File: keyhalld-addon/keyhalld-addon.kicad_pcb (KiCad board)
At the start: 2 copper layers, 44 parts, among them J1 Conn_01x06_Pin, J2 Conn_01x04_Pin, SW1 SW_Push, SW2 SW_Push, SW3 SW_Push, SW4 SW_Push, SW5 SW_Push, SW6 SW_Push, SW7 SW_Push, SW8 SW_Push, U1 RP2350A, U2 ER_OLEDM0.91_1x-I2C, U22 TLV1117-33, Y1 12MHz

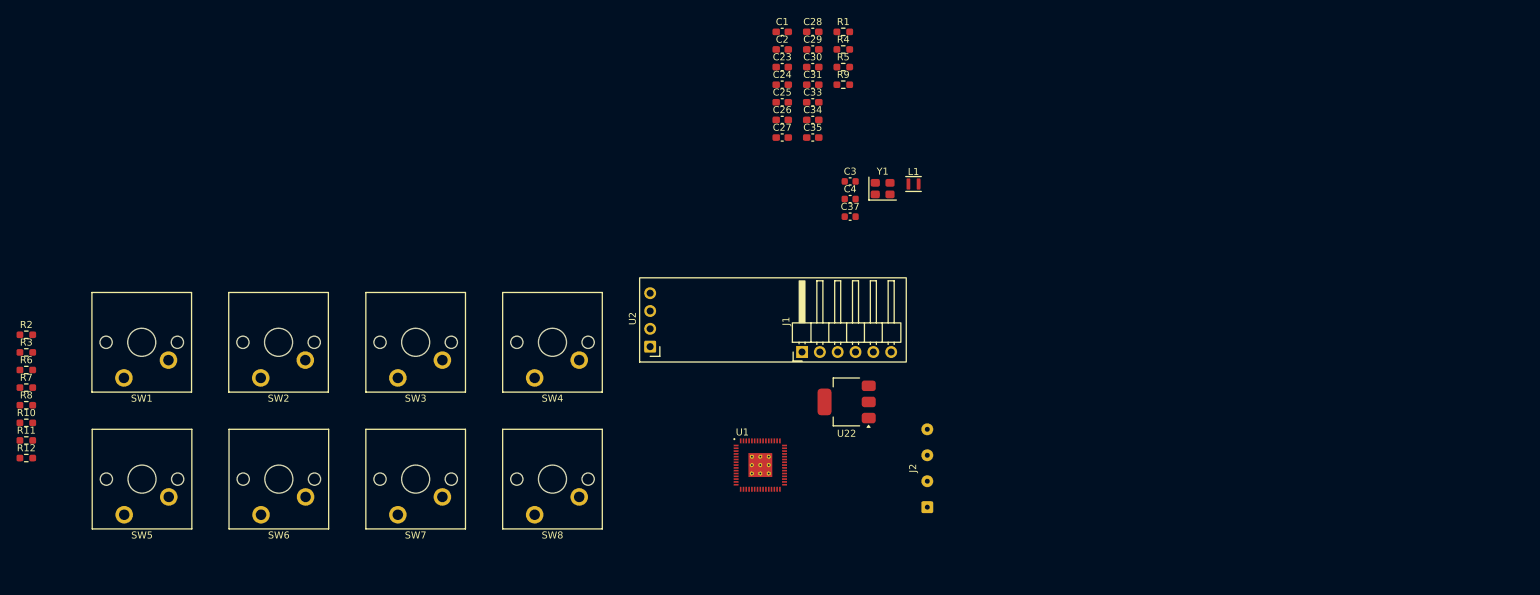
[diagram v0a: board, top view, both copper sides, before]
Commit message: add local fp for cherry mx mech switch
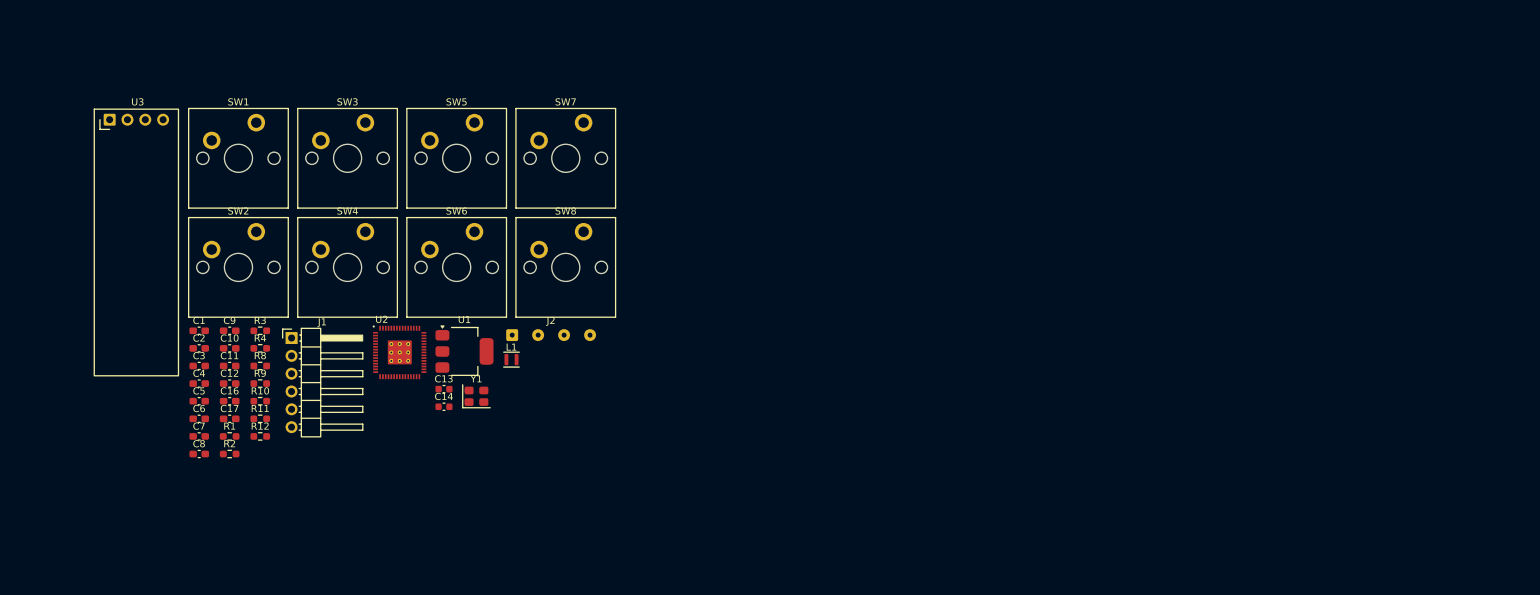
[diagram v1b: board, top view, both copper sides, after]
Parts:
- removed C23, C24, C25, C26, C27, C28, C29, C30, C33, C34: 100n, Capacitor_SMD:C_0603_1608Metric_Pad1.08x0.95mm_HandSolder
- removed C31, C35: 1u, Capacitor_SMD:C_0603_1608Metric_Pad1.08x0.95mm_HandSolder
- removed C37: 4.7u, Capacitor_SMD:C_0603_1608Metric
- removed R5: 22R, Resistor_SMD:R_0603_1608Metric_Pad0.98x0.95mm_HandSolder
- removed R6, R7: 10K, Resistor_SMD:R_0603_1608Metric_Pad0.98x0.95mm_HandSolder
- removed U22: TLV1117-33, Package_TO_SOT_SMD:SOT-223
- added C10: 100n, Capacitor_SMD:C_0603_1608Metric_Pad1.08x0.95mm_HandSolder, F.Cu at (75.1, 86.4)
- added C11: 1u, Capacitor_SMD:C_0603_1608Metric_Pad1.08x0.95mm_HandSolder, F.Cu at (75.1, 88.9)
- added C12: 1u, Capacitor_SMD:C_0603_1608Metric_Pad1.08x0.95mm_HandSolder, F.Cu at (75.1, 91.4)
- added C13: 4.7u, Capacitor_SMD:C_0603_1608Metric, F.Cu at (105.6, 92.2)
- added C14: 4.7u, Capacitor_SMD:C_0603_1608Metric, F.Cu at (105.6, 94.7)
- added C16: 15p, Capacitor_SMD:C_0603_1608Metric_Pad1.08x0.95mm_HandSolder, F.Cu at (75.1, 93.9)
- added C17: 15p, Capacitor_SMD:C_0603_1608Metric_Pad1.08x0.95mm_HandSolder, F.Cu at (75.1, 96.4)
- added C5: 100n, Capacitor_SMD:C_0603_1608Metric_Pad1.08x0.95mm_HandSolder, F.Cu at (70.7, 93.9)
- added C6: 100n, Capacitor_SMD:C_0603_1608Metric_Pad1.08x0.95mm_HandSolder, F.Cu at (70.7, 96.4)
- added C7: 100n, Capacitor_SMD:C_0603_1608Metric_Pad1.08x0.95mm_HandSolder, F.Cu at (70.7, 98.9)
- added C8: 100n, Capacitor_SMD:C_0603_1608Metric_Pad1.08x0.95mm_HandSolder, F.Cu at (70.7, 101.4)
- added C9: 100n, Capacitor_SMD:C_0603_1608Metric_Pad1.08x0.95mm_HandSolder, F.Cu at (75.1, 83.9)
- added U3: ER_OLEDM0.91_1x-I2C, Display:ER_OLEDM0.91_1x-I2C, F.Cu at (58.0, 53.8)
- C1, C2: value 15p -> 100n
- C3, C4: value 4.7u -> 100n; footprint Capacitor_SMD:C_0603_1608Metric -> Capacitor_SMD:C_0603_1608Metric_Pad1.08x0.95mm_HandSolder
- R1: value 1K -> 10K
- R12: value 10K -> 1K
- R4: value 22R -> 10K
- R9: value 33 -> 10K
- SW1, SW2, SW3, SW4, SW5, SW6, SW7, SW8: footprint Switch_Keyboard_Cherry_MX:SW_Cherry_MX_PCB_1.00u -> Library:SW_Cherry_MX_PCB_1.00u
- U1: value RP2350A -> TLV1117-33; footprint RPI:rpi_rp2350a_vias -> Package_TO_SOT_SMD:SOT-223
- U2: value ER_OLEDM0.91_1x-I2C -> RP2350A; footprint Display:ER_OLEDM0.91_1x-I2C -> RPI:rpi_rp2350a_vias
- moved R1 104.7 mm to (75.1, 98.9)
- moved C3 96.4 mm to (70.7, 88.9)
- moved C4 96.4 mm to (70.7, 91.4)
- moved R9 93.4 mm to (79.4, 91.4)
- moved C1 93.4 mm to (70.7, 83.9)
- moved C2 93.4 mm to (70.7, 86.4)
- moved R4 93.4 mm to (79.4, 86.4)
- moved J1 72.8 mm to (83.9, 84.9), turned to 0 degrees
- moved Y1 65.0 mm to (110.2, 93.2)
- moved J2 64.0 mm to (115.3, 84.5), turned to 0 degrees
- moved SW5 64.0 mm to (107.4, 59.3), turned to 0 degrees
- moved L1 62.5 mm to (115.2, 88.0)
- moved SW7 50.5 mm to (123.0, 59.3), turned to 0 degrees
- moved U1 45.2 mm to (108.5, 86.8)
- moved SW6 39.4 mm to (107.4, 74.8), turned to 0 degrees
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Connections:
- C1 pad 1: GND -> +3.3V
- C1 pad 2: XIN -> GND
- C2 pad 1: GND -> +3.3V
- C2 pad 2: Net-(C2-Pad2) -> GND
- C3 pad 1: +1V1 -> +3.3V
- L1 pad 2: Net-(U1-VREG_LX) -> Net-(U2-VREG_LX)
- R1 pad 1: XOUT -> +3.3V
- R1 pad 2: Net-(C2-Pad2) -> KEY1
- R10 pad 2: KEY6 -> KEY7
- R11 pad 2: KEY7 -> KEY8
- R12 pad 1: +3.3V -> XOUT
- R12 pad 2: KEY8 -> Net-(C17-Pad2)
- R2 pad 2: KEY1 -> KEY2
- R3 pad 2: KEY2 -> KEY3
- R4 pad 1: Net-(U1-USB_DP) -> +3.3V
- R4 pad 2: D+ -> KEY4
- R9 pad 1: Net-(U1-VREG_AVDD) -> +3.3V
- R9 pad 2: +3.3VA -> KEY6
- U1 pad 1: +3.3V -> GND
- U1 pad 2: DBG_TX -> +3.3V
- U1 pad 3: unconnected-(U1-GPIO1-Pad3) -> +5V
- U1 pad 4: unconnected-(U1-GPIO2-Pad4) -> (no net)
- U2 pad 1: GND -> +3.3V
- U2 pad 2: +3.3V -> DBG_TX
- U2 pad 3: OLED_SCL -> unconnected-(U2-GPIO1-Pad3)
- U2 pad 4: OLED_SDA -> unconnected-(U2-GPIO2-Pad4)
- Y1 pad 3: Net-(C2-Pad2) -> Net-(C17-Pad2)

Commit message: fix some custom fp; change fp for mech keys to hotswap
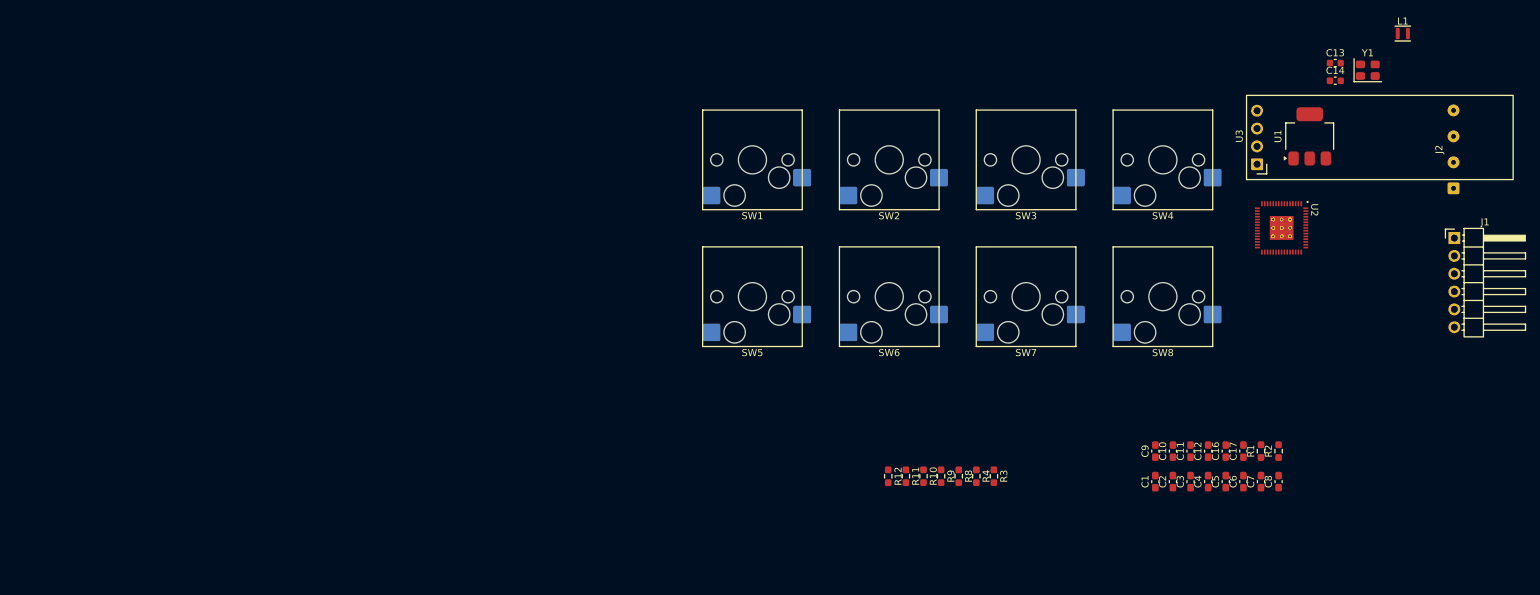
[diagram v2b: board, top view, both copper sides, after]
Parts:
- SW1, SW2, SW3, SW4, SW5, SW6, SW7, SW8: footprint Library:SW_Cherry_MX_PCB_1.00u -> Library:SW_Hotswap_Kailh_MX_1.00u
- moved J1 166.3 mm to (249.6, 70.7)
- moved U3 163.7 mm to (221.5, 60.1), turned to 90 degrees
- moved C8 153.9 mm to (224.6, 105.4), turned to 90 degrees
- moved C7 151.5 mm to (222.1, 105.4), turned to 90 degrees
- moved R2 149.5 mm to (224.6, 101.0), turned to 90 degrees
- moved C6 149.1 mm to (219.6, 105.4), turned to 90 degrees
- moved R1 147.0 mm to (222.1, 101.0), turned to 90 degrees
- moved C5 146.8 mm to (217.0, 105.4), turned to 90 degrees
- moved C17 144.5 mm to (219.6, 101.0), turned to 90 degrees
- moved C4 144.5 mm to (214.5, 105.4), turned to 90 degrees
- moved C3 142.3 mm to (212.0, 105.4), turned to 90 degrees
- moved C16 142.1 mm to (217.0, 101.0), turned to 90 degrees
- moved C2 140.1 mm to (209.5, 105.4), turned to 90 degrees
- moved C12 139.8 mm to (214.5, 101.0), turned to 90 degrees
- moved C1 138.0 mm to (207.0, 105.4), turned to 90 degrees
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
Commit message: add option for usb connection to addon board; initial addon pcb layout
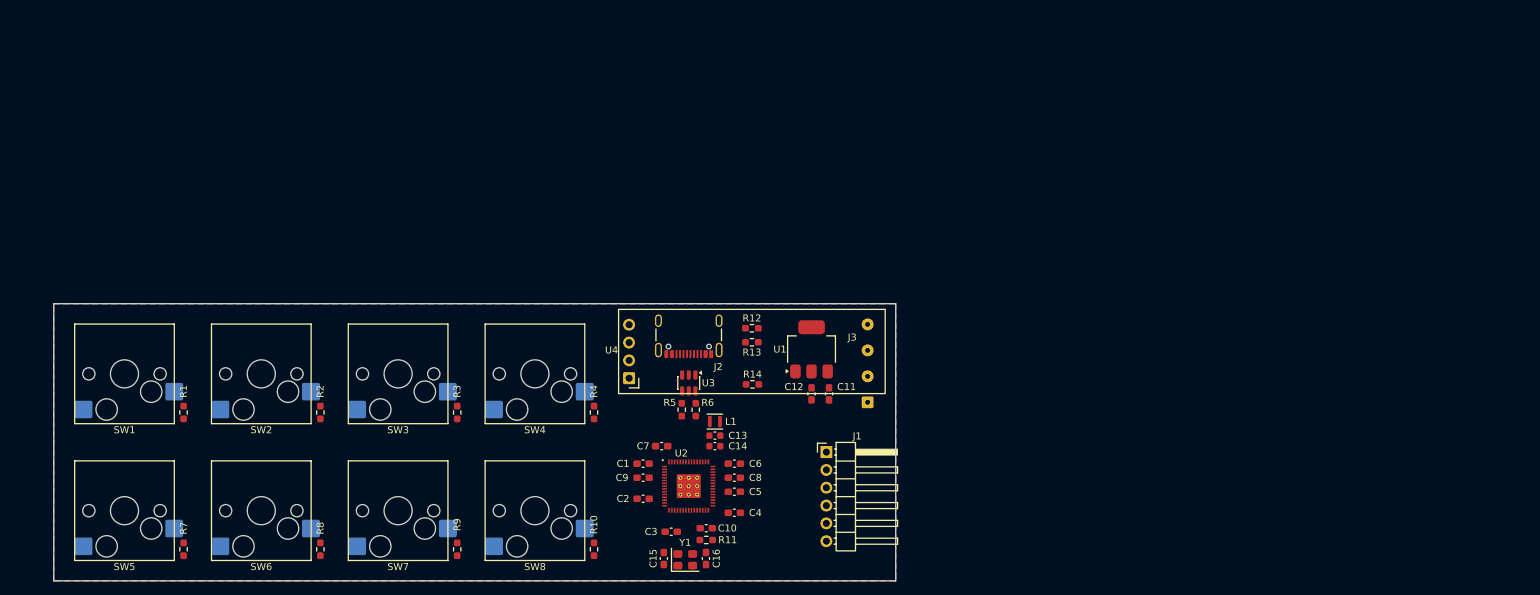
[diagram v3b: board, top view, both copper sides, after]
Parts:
- added J2: USB_C_Receptacle_USB2.0_16P, Connector_USB:USB_C_Receptacle_GCT_USB4105-xx-A_16P_TopMnt_Horizontal, F.Cu at (140.5, 83.5)
- added R12: 5K1, Resistor_SMD:R_0603_1608Metric_Pad0.98x0.95mm_HandSolder, F.Cu at (149.5, 83.5)
- added R13: 5K1, Resistor_SMD:R_0603_1608Metric_Pad0.98x0.95mm_HandSolder, F.Cu at (149.5, 85.5)
- added R14: 1.5K, Resistor_SMD:R_0603_1608Metric_Pad0.98x0.95mm_HandSolder, F.Cu at (149.6, 91.5)
- added R5: 22R, Resistor_SMD:R_0603_1608Metric_Pad0.98x0.95mm_HandSolder, F.Cu at (139.5, 95.1)
- added R6: 22R, Resistor_SMD:R_0603_1608Metric_Pad0.98x0.95mm_HandSolder, F.Cu at (141.5, 95.1)
- added U3: USBLC6-2SC6, Package_TO_SOT_SMD:SOT-23-6, F.Cu at (140.5, 91.3)
- moved R1 153.7 mm to (68.5, 95.5)
- moved R2 136.7 mm to (88.0, 95.5)
- moved Y1 119.7 mm to (140.0, 116.5)
- moved L1 112.6 mm to (144.2, 96.8), turned to 180 degrees
- moved R7 111.0 mm to (68.5, 115.0), turned to 90 degrees
- moved C13 103.1 mm to (144.2, 98.8), turned to 180 degrees
- moved C14 102.6 mm to (144.2, 100.3), turned to 180 degrees
- moved SW1 94.6 mm to (60.1, 90.0)
- moved SW2 94.6 mm to (79.6, 90.0)
- moved SW3 94.6 mm to (99.1, 90.0)
- moved SW4 94.6 mm to (118.6, 90.0)
- moved SW5 94.6 mm to (60.1, 109.5)
- moved SW6 94.6 mm to (79.6, 109.5)
- moved SW7 94.6 mm to (99.1, 109.5)
- moved SW8 94.6 mm to (118.6, 109.5)
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- renumbered C16 to C15, C17 to C16, J2 to J3, R11 to R10, R12 to R11, R8 to R7, R9 to R8, R10 to R9, U3 to U4
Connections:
- U2 pad 51: unconnected-(U2-USB_DM-Pad51) -> Net-(U2-USB_DM)
- U2 pad 52: unconnected-(U2-USB_DP-Pad52) -> Net-(U2-USB_DP)
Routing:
- added copper zone on B.Cu, net GND
- added copper zone on F.Cu, net GND
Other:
- board outline added: 120 x 39.5 mm

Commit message: small adjustments
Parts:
- moved J1 6.77 mm to (166.0, 104.5)
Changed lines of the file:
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@@
 	)
 	(setup
+		(stackup
+			(layer "F.SilkS"
+				(type "Top Silk Screen")
+			)
+			(layer "F.Paste"
+				(type "Top Solder Paste")
+			)
+			(layer "F.Mask"
+				(type "Top Solder Mask")
+				(thickness 0.01)
+			)
+			(layer "F.Cu"
+				(type "copper")
+				(thickness 0.035)
+			)
+			(layer "dielectric 1"
+				(type "core")
+				(thickness 1.51)
+				(material "FR4")
+				(epsilon_r 4.5)
+				(loss_tangent 0.02)
+			)
+			(layer "B.Cu"
+				(type "copper")
+				(thickness 0.035)
+			)
+			(layer "B.Mask"
+				(type "Bottom Solder Mask")
+				(thickness 0.01)
+			)
+			(layer "B.Paste"
+				(type "Bottom Solder Paste")
+			)
+			(layer "B.SilkS"
+				(type "Bottom Silk Screen")
+			)
+			(copper_finish "None")
+			(dielectric_constraints no)
+		)
 		(pad_to_mask_clearance 0)
 		(allow_soldermask_bridges_in_footprints no)
@@
 		(capping no)
 		(filling no)
+		(zone_defaults)
 		(pcbplotparams
 			(layerselection 0x00000000_00000000_55555555_5755f5ff)
@@
 	(footprint "Connector_PinHeader_2.54mm:PinHeader_1x06_P2.54mm_Horizontal"
 		(layer "F.Cu")
-		(at 160.115 101.15)
+		(at 166 104.5)
 		(descr "Through hole angled pin header, 1x06, 2.54mm pitch, 6mm pin length, single row")
 		(tags "Through hole angled pin header THT 1x06 2.54mm single row")

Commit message: route addon board
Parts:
- moved R1 62.1 mm to (130.0, 104.4)
- moved R7 61.9 mm to (130.0, 108.1), turned to -90 degrees
- moved R2 44.9 mm to (132.0, 104.4)
- moved R8 44.5 mm to (132.0, 108.1), turned to -90 degrees
- moved R3 28.0 mm to (134.0, 104.4)
- moved R9 27.4 mm to (134.0, 108.1), turned to -90 degrees
- moved R4 12.6 mm to (136.0, 104.3)
- moved R10 11.3 mm to (136.0, 108.1), turned to -90 degrees
- moved C3 10.0 mm to (148.0, 113.5)
- moved C1 10.0 mm to (144.0, 102.5)
- moved C7 10.0 mm to (146.6, 100.0)
- moved C9 10.0 mm to (144.0, 104.5)
- moved C10 10.0 mm to (153.0, 112.0)
- moved C15 10.0 mm to (146.9, 116.3)
- moved C16 10.0 mm to (152.9, 116.3)
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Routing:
- net +3.3V: track 0.00 -> 109.5 mm, vias 0 -> 12
- net KEY1: track 0.00 -> 89.8 mm, vias 0 -> 2
- net KEY5: track 0.00 -> 86.8 mm, vias 0 -> 2
- net KEY2: track 0.00 -> 71.6 mm, vias 0 -> 2
- net KEY6: track 0.00 -> 68.6 mm, vias 0 -> 2
- net KEY3: track 0.00 -> 53.1 mm, vias 0 -> 2
- net KEY7: track 0.00 -> 50.5 mm, vias 0 -> 2
- net GND: track 0.00 -> 49.8 mm, vias 0 -> 30
- net +5V: track 0.00 -> 44.5 mm, vias 0 -> 5
- net MAG_UART_RX: track 0.00 -> 35.9 mm, vias 0 -> 3
- net MAG_UART_TX: track 0.00 -> 33.6 mm, vias 0 -> 1
- net KEY4: track 0.00 -> 32.6 mm, vias 0 -> 2
- net OLED_SDA: track 0.00 -> 30.0 mm, vias 0 -> 1
- net KEY8: track 0.00 -> 28.3 mm, vias 0 -> 2
- net OLED_SCL: track 0.00 -> 28.2 mm, vias 0 -> 1
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- added copper zone on F.Cu, net +1V1
- added copper zone on In1.Cu, net +1V1
- added copper zone on F.Cu, net +3.3V
- added copper zone on In1.Cu, net +3.3V
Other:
- copper layers 2 -> 4
